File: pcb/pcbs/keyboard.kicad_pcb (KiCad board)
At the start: 2 copper layers, 152.4 x 110.9 mm, 96 parts, among them J1 Jumper, J10 Jumper, J11 Jumper, J12 Jumper, J13 Jumper, J14 Jumper, J15 Jumper, J16 Jumper, J17 Jumper, J18 Jumper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

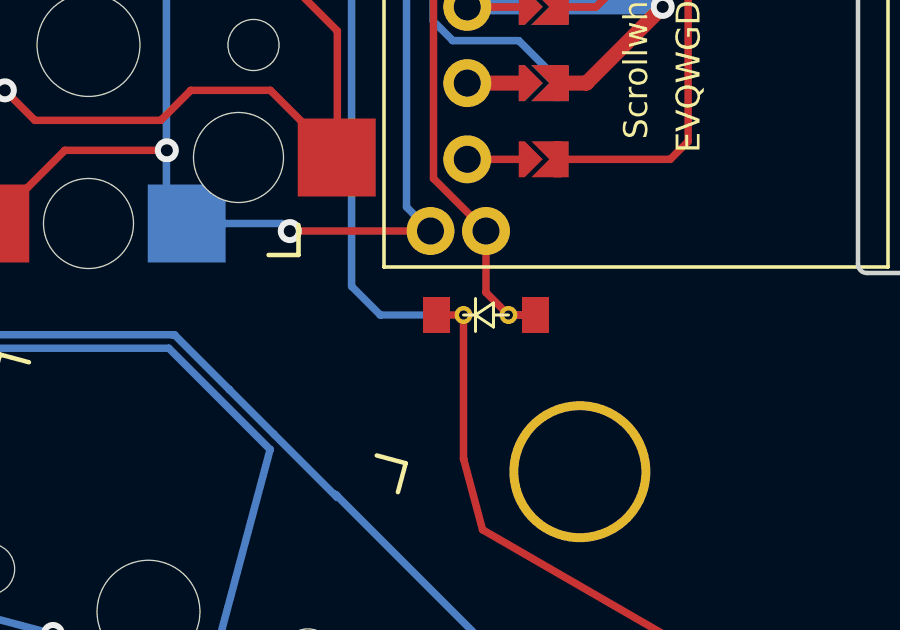
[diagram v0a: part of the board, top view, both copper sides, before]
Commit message: add missing connection
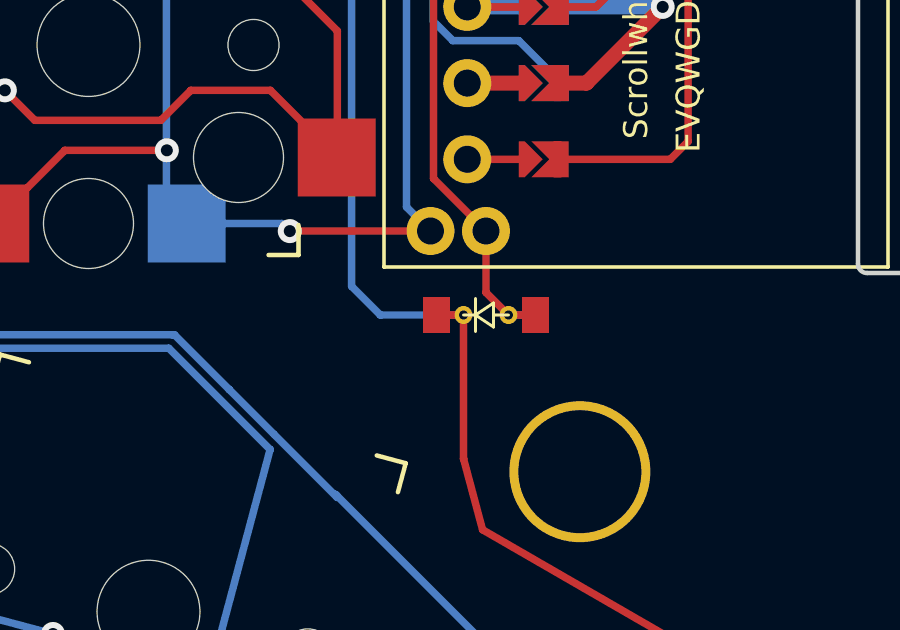
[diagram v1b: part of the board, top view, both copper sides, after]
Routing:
- net col4: track 150.0 -> 150.9 mm
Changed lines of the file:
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@@
   (segment (start 162.322084 78.337895) (end 162.047084 78.612895) (width 0.25) (layer "B.Cu") (net 37))
   (segment (start 162.596553 78.029415) (end 162.322084 78.303884) (width 0.25) (layer "B.Cu") (net 37))
+  (segment (start 165.780485 105.525879) (end 164.880485 105.525879) (width 0.25) (layer "B.Cu") (net 37))
   (segment (start 175.387188 117.863402) (end 174.607771 117.413397) (width 0.25) (layer "B.Cu") (net 37))
   (segment (start 115.626237 114.423931) (end 116.526241 114.423929) (width 0.25) (layer "B.Cu") (net 37))

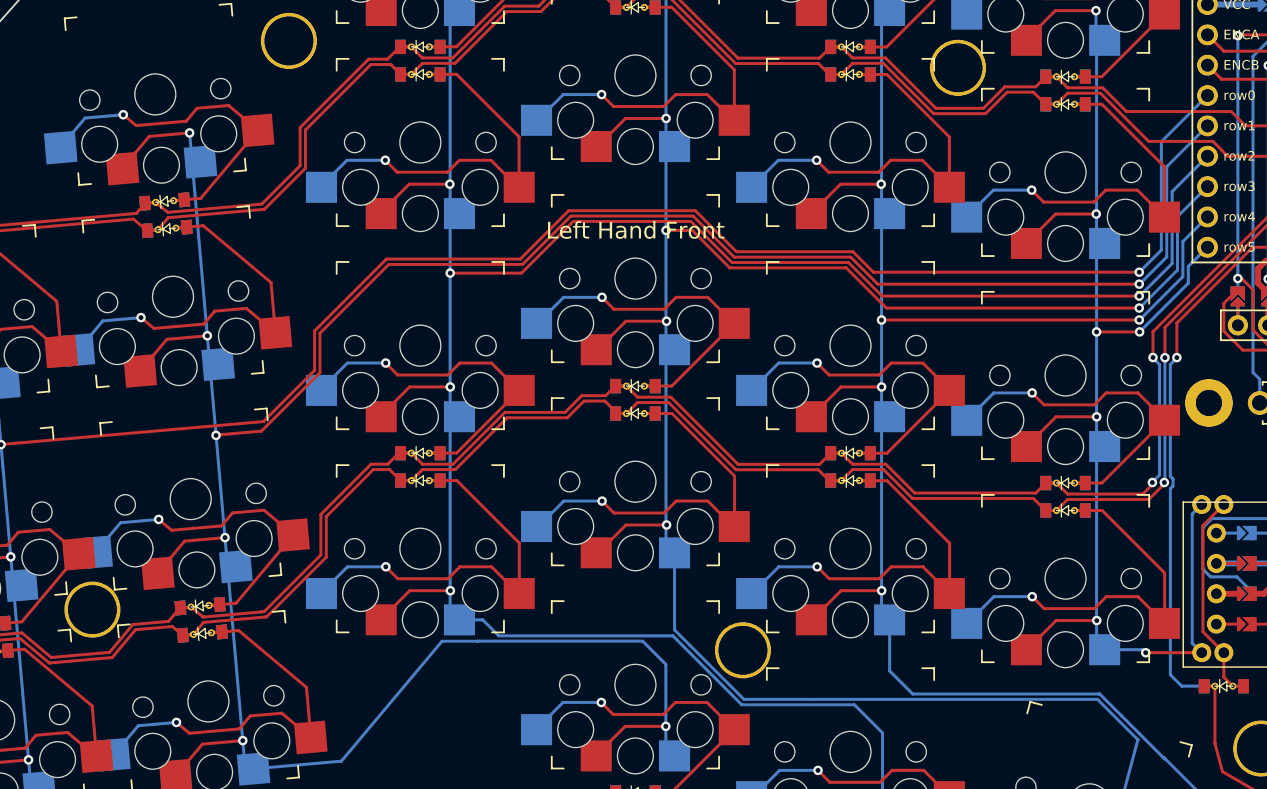
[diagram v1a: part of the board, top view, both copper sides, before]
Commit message: add ground vias
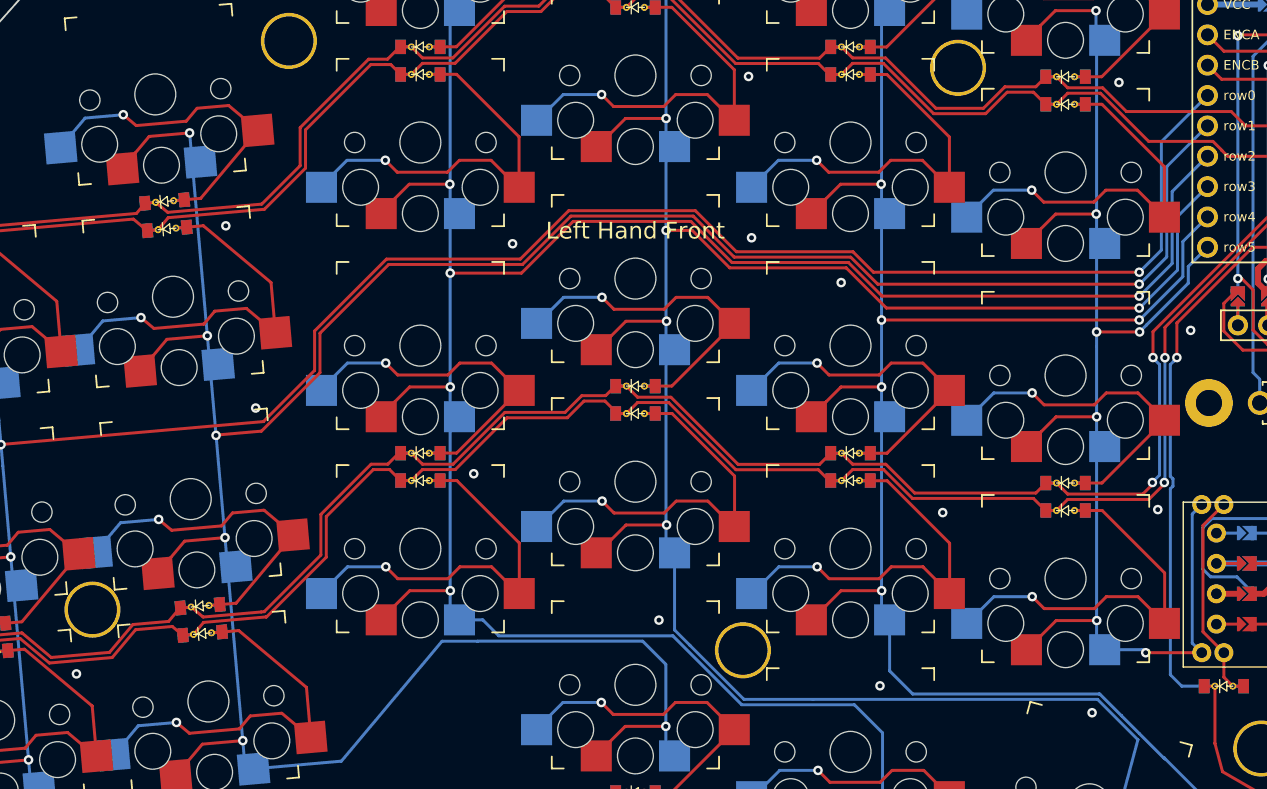
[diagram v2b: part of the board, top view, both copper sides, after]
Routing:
- net GND: vias 3 -> 18
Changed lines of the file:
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@@
   (segment (start 169.880015 97.795882) (end 169.038494 97.795882) (width 0.5) (layer "F.Cu") (net 46))
   (segment (start 172.422256 85.434148) (end 179.610499 78.245905) (width 0.5) (layer "F.Cu") (net 46))
+  (via (at 163.75 75.75) (size 0.8) (drill 0.4) (layers "F.Cu" "B.Cu") (free) (net 46))
   (via (at 172.42 95.255897) (size 0.8) (drill 0.4) (layers "F.Cu" "B.Cu") (net 46))
+  (via (at 155.5 107.75) (size 0.8) (drill 0.4) (layers "F.Cu" "B.Cu") (free) (net 46))
+  (via (at 103.75 87.75) (size 0.8) (drill 0.4) (layers "F.Cu" "B.Cu") (free) (net 46))
   (via (at 173.547683 44.782957) (size 0.8) (drill 0.4) (layers "F.Cu" "B.Cu") (net 46))
+  (via (at 85.5 82.25) (size 0.8) (drill 0.4) (layers "F.Cu" "B.Cu") (free) (net 46))
+  (via (at 83 67) (size 0.8) (drill 0.4) (layers "F.Cu" "B.Cu") (free) (net 46))
+  (via (at 137.75 105.5) (size 0.8) (drill 0.4) (layers "F.Cu" "B.Cu") (free) (net 46))
+  (via (at 143 91) (size 0.8) (drill 0.4) (layers "F.Cu" "B.Cu") (free) (net 46))
+  (via (at 126.75 54.5) (size 0.8) (drill 0.4) (layers "F.Cu" "B.Cu") (free) (net 46))
+  (via (at 107 68.5) (size 0.8) (drill 0.4) (layers "F.Cu" "B.Cu") (free) (net 46))
+  (via (at 157.75 55) (size 0.8) (drill 0.4) (layers "F.Cu" "B.Cu") (free) (net 46))
+  (via (at 161 90.75) (size 0.8) (drill 0.4) (layers "F.Cu" "B.Cu") (free) (net 46))
+  (via (at 134.5 71.75) (size 0.8) (drill 0.4) (layers "F.Cu" "B.Cu") (free) (net 46))
+  (via (at 70.5 104.5) (size 0.8) (drill 0.4) (layers "F.Cu" "B.Cu") (free) (net 46))
   (via (at 175.320492 69.932953) (size 0.8) (drill 0.4) (layers "F.Cu" "B.Cu") (net 46))
+  (via (at 127 68) (size 0.8) (drill 0.4) (layers "F.Cu" "B.Cu") (free) (net 46))
+  (via (at 119.25 100) (size 0.8) (drill 0.4) (layers "F.Cu" "B.Cu") (free) (net 46))
   (segment (start 177.247691 41.108693) (end 180.530498 37.82588) (width 0.5) (layer "B.Cu") (net 46))
   (segment (start 172.42 95.255897) (end 169.038495 95.255897) (width 0.5) (layer "B.Cu") (net 46))

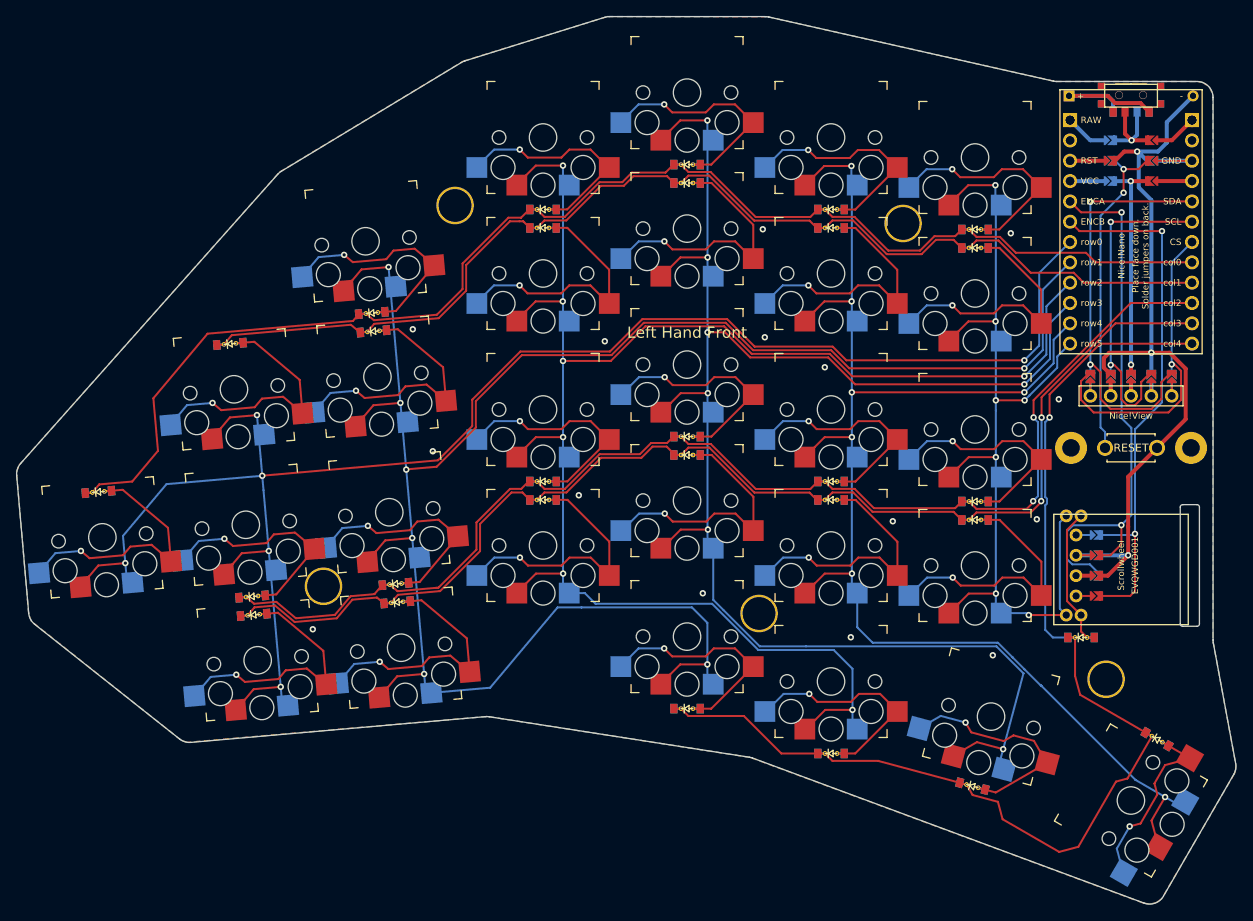
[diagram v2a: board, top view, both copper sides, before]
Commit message: add more ground vias
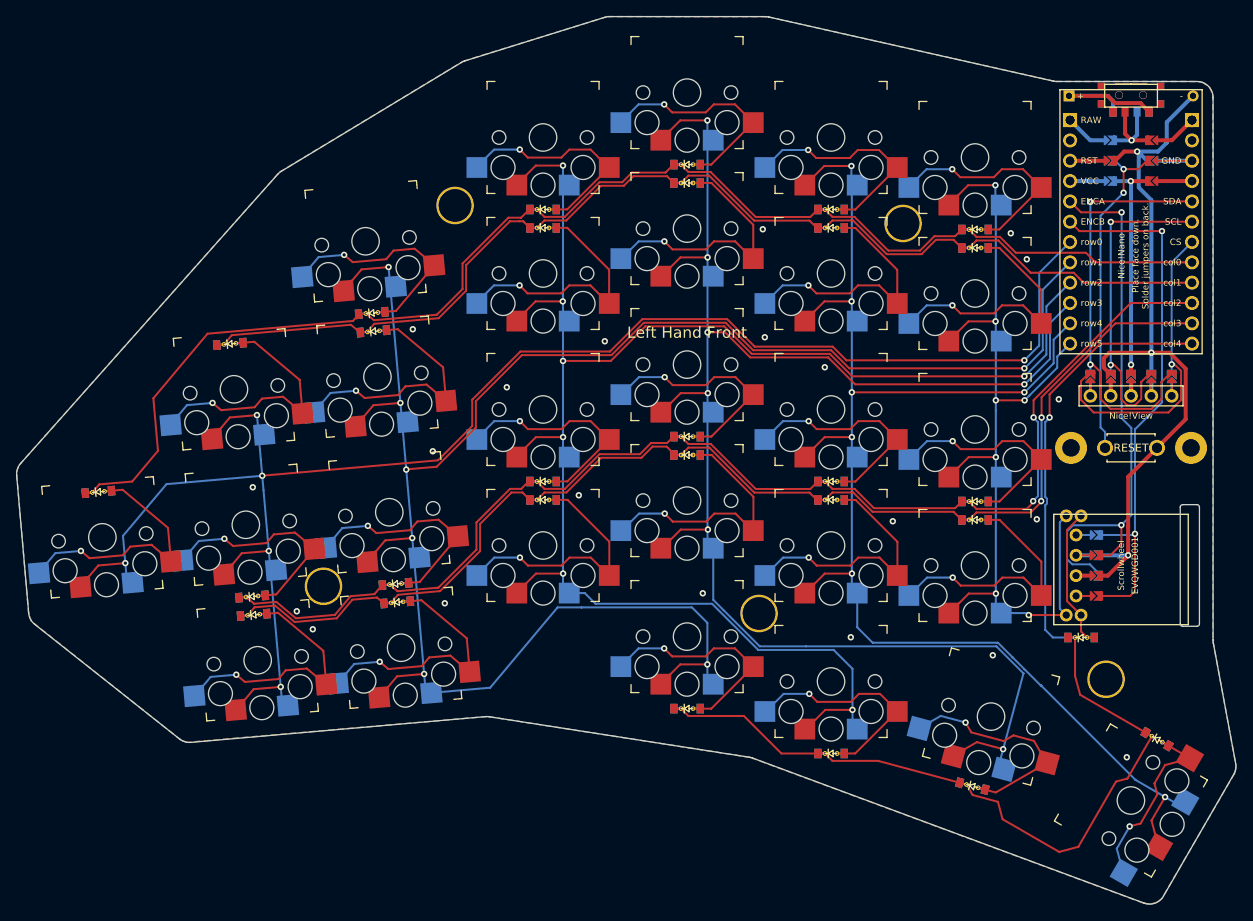
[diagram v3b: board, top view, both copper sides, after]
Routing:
- net GND: vias 18 -> 24
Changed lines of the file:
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@@
   (segment (start 172.422256 85.434148) (end 179.610499 78.245905) (width 0.5) (layer "F.Cu") (net 46))
   (via (at 163.75 75.75) (size 0.8) (drill 0.4) (layers "F.Cu" "B.Cu") (free) (net 46))
+  (via (at 94.75 74.25) (size 0.8) (drill 0.4) (layers "F.Cu" "B.Cu") (free) (net 46))
+  (via (at 68.5 102.25) (size 0.8) (drill 0.4) (layers "F.Cu" "B.Cu") (free) (net 46))
   (via (at 172.42 95.255897) (size 0.8) (drill 0.4) (layers "F.Cu" "B.Cu") (net 46))
   (via (at 155.5 107.75) (size 0.8) (drill 0.4) (layers "F.Cu" "B.Cu") (free) (net 46))
@@
   (via (at 107 68.5) (size 0.8) (drill 0.4) (layers "F.Cu" "B.Cu") (free) (net 46))
   (via (at 157.75 55) (size 0.8) (drill 0.4) (layers "F.Cu" "B.Cu") (free) (net 46))
+  (via (at 87 101.25) (size 0.8) (drill 0.4) (layers "F.Cu" "B.Cu") (free) (net 46))
   (via (at 161 90.75) (size 0.8) (drill 0.4) (layers "F.Cu" "B.Cu") (free) (net 46))
+  (via (at 159.75 58.25) (size 0.8) (drill 0.4) (layers "F.Cu" "B.Cu") (free) (net 46))
   (via (at 134.5 71.75) (size 0.8) (drill 0.4) (layers "F.Cu" "B.Cu") (free) (net 46))
   (via (at 70.5 104.5) (size 0.8) (drill 0.4) (layers "F.Cu" "B.Cu") (free) (net 46))
+  (via (at 63 86.75) (size 0.8) (drill 0.4) (layers "F.Cu" "B.Cu") (free) (net 46))
   (via (at 175.320492 69.932953) (size 0.8) (drill 0.4) (layers "F.Cu" "B.Cu") (net 46))
   (via (at 127 68) (size 0.8) (drill 0.4) (layers "F.Cu" "B.Cu") (free) (net 46))
   (via (at 119.25 100) (size 0.8) (drill 0.4) (layers "F.Cu" "B.Cu") (free) (net 46))
+  (via (at 172.25 120.5) (size 0.8) (drill 0.4) (layers "F.Cu" "B.Cu") (free) (net 46))
   (segment (start 177.247691 41.108693) (end 180.530498 37.82588) (width 0.5) (layer "B.Cu") (net 46))
   (segment (start 172.42 95.255897) (end 169.038495 95.255897) (width 0.5) (layer "B.Cu") (net 46))

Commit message: add order pcb number
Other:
- board text added: "JLCJLCJLCJLC"
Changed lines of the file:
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@@
   (gr_arc (start 183.064029 106.206719) (mid 183.038892 106.025112) (end 183.030495 105.841966)
     (stroke (width 0.15) (type solid)) (layer "Edge.Cuts"))
+  (gr_text "JLCJLCJLCJLC" (at 162.5 131 -20) (layer "B.SilkS")
+    (effects (font (size 0.5 0.5) (thickness 0.1) bold) (justify left bottom mirror))
+  )
   (segment (start 42.536333 97.89179) (end 43.680943 96.527693) (width 0.25) (layer "F.Cu") (net 1))
   (segment (start 137.197687 70.88295) (end 135.484737 69.17) (width 0.25) (layer "F.Cu") (net 1))
